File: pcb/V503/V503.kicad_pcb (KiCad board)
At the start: 4 copper layers, 77.3 x 153.4 mm, 32 parts, among them J1 Conn_01x20_Pin, J2 Conn_01x20_Pin, J3 Conn_01x20_Pin, J4 Conn_01x20_Pin, U1 74LS670, U10 74LS283, U11 74LS245, U12 74LS245, U13 74LS245, U14 74LS245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

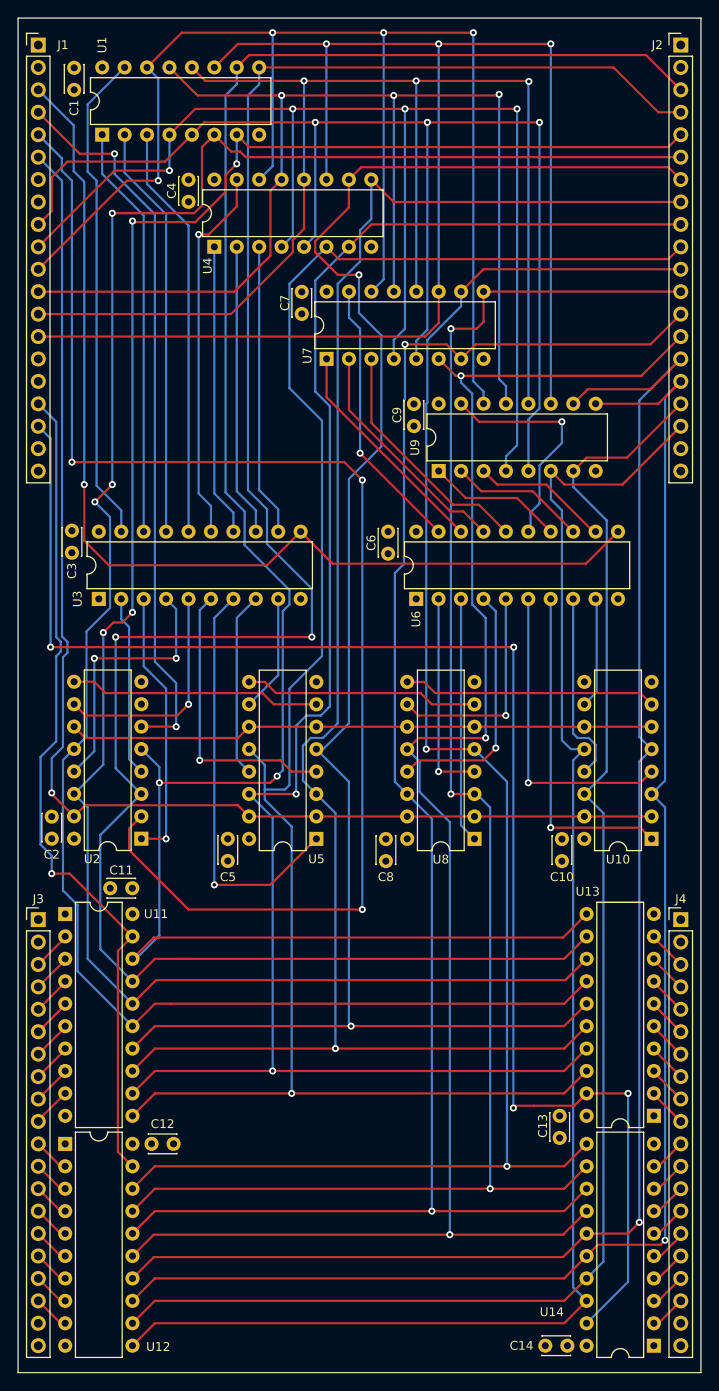
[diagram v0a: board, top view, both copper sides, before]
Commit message: Clean up clearances, run DRC and ERC, and generate Gerbers. Tape out.
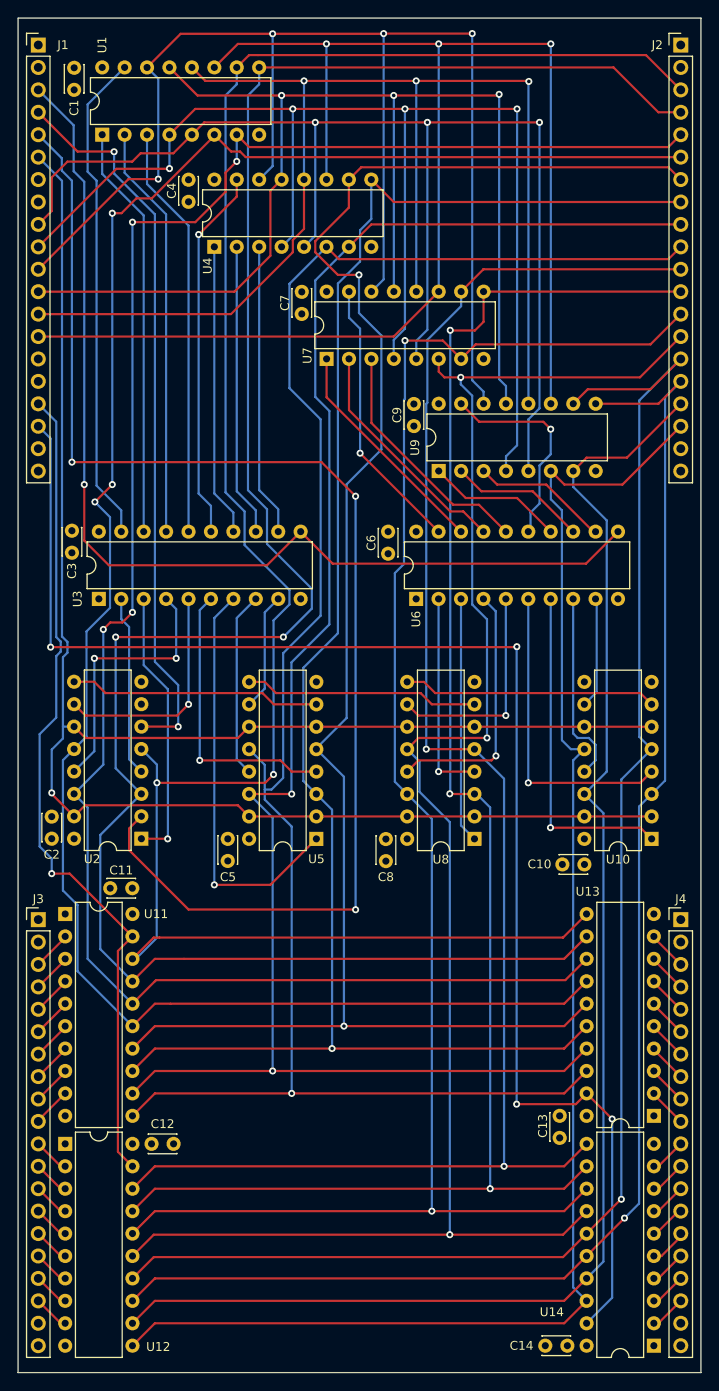
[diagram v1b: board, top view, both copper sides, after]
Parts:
- moved C10 3.84 mm to (98.3, 123.9), turned to 180 degrees
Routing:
- net SYSADDR13: track 173.1 -> 167.7 mm
- net ~{AtoD}: track 171.9 -> 167.1 mm
- net SYSADDR3: track 225.6 -> 221.8 mm
- net SYSADDR12: track 175.2 -> 172.5 mm
- net SRC2:1: track 154.6 -> 152.1 mm
- net HLD12: track 26.3 -> 24.0 mm
- net ~{Er}: track 172.9 -> 170.9 mm
- net SYSADDR1: track 237.3 -> 235.4 mm
- net SYSADDR6: track 196.8 -> 195.5 mm
- net SRC2:2: track 210.7 -> 212.0 mm
- net SYSADDR11: track 192.2 -> 193.2 mm
- net SYSADDR7: track 204.6 -> 203.5 mm
- net SYSADDR5: track 193.6 -> 192.6 mm
- net SYSADDR4: track 199.4 -> 198.6 mm
- net HLD4: track 42.9 -> 42.3 mm
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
